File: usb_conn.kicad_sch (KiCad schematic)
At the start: 16 parts, among them U13 DLM0NSN500HY2D, U6 TPUSBLC6-4SC6

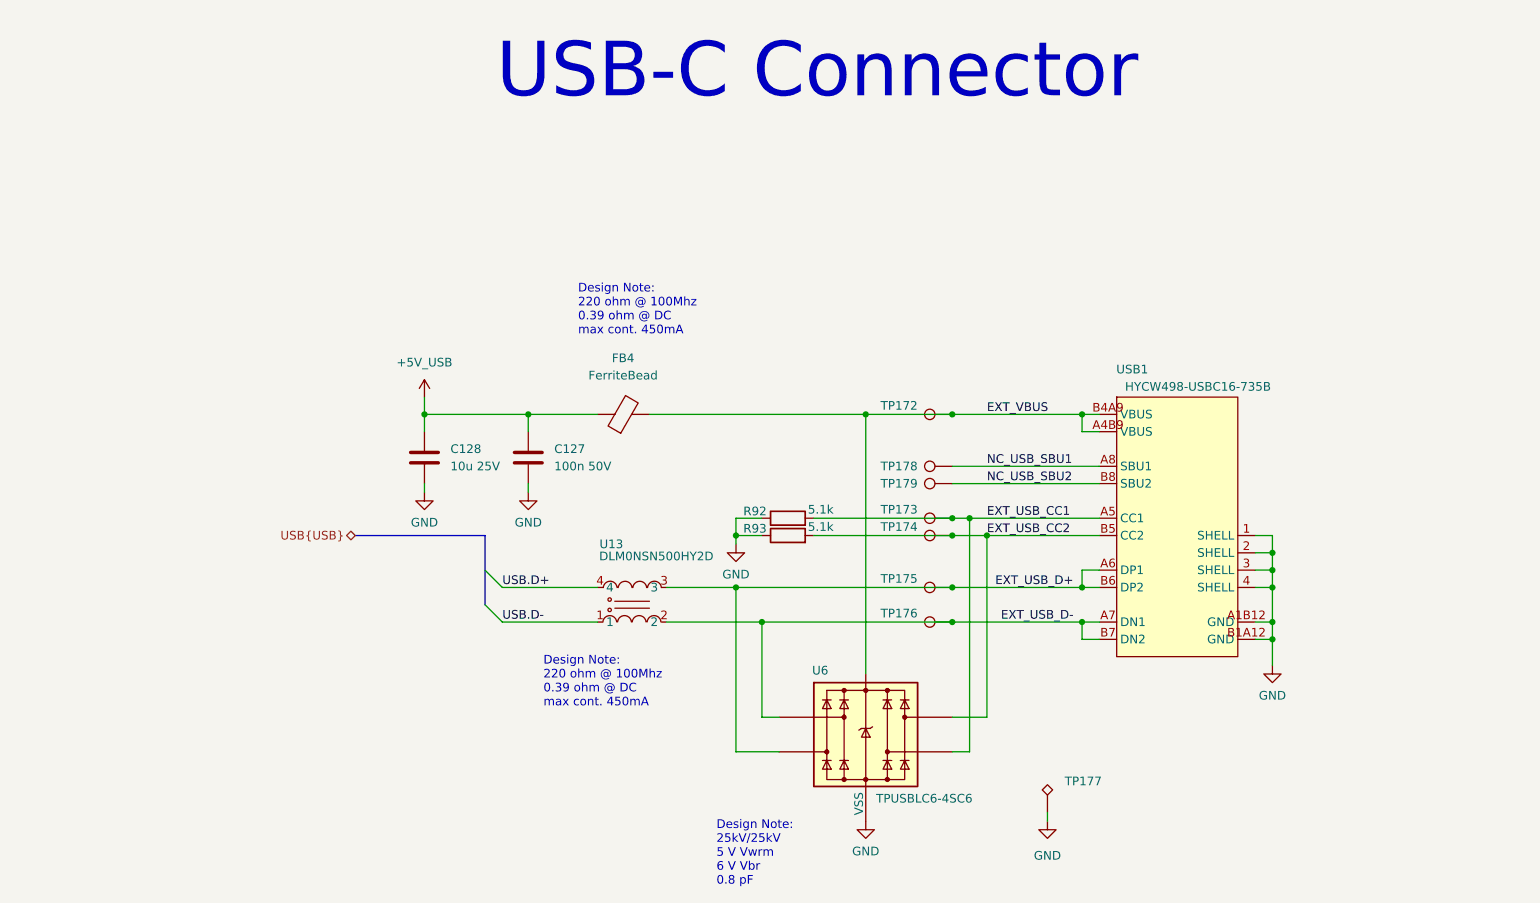
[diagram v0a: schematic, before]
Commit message: did stuff, amongst others changed to op-amp input filter
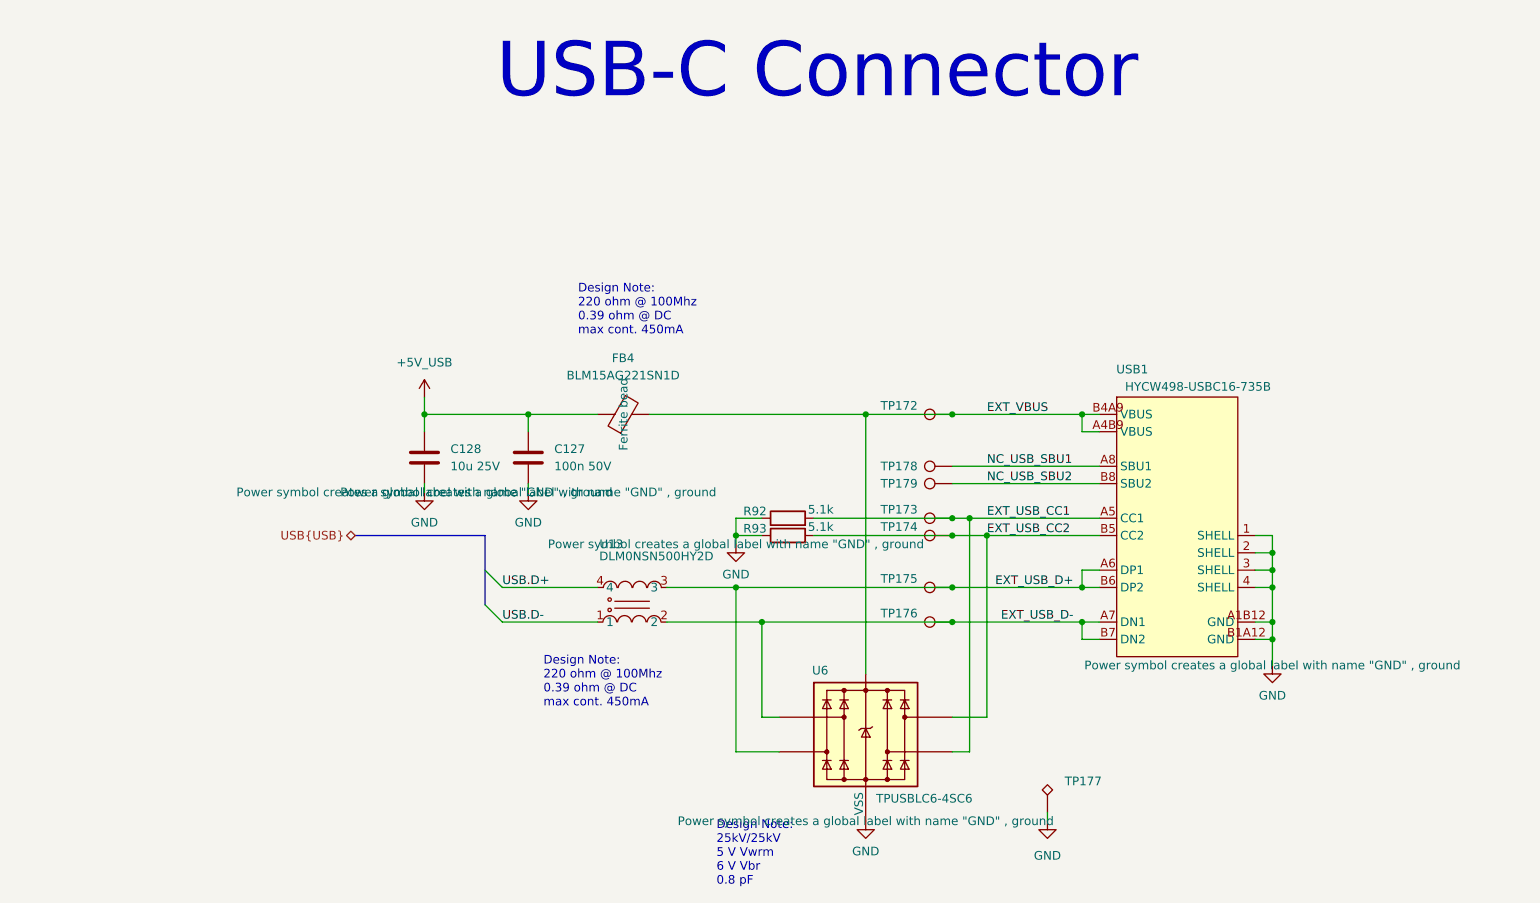
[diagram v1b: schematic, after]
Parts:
- FB4: value FerriteBead -> BLM15AG221SN1D; LCSC Part (none) -> C85813
- U13: LCSC (none) -> C913480
- USB1: LCSC (none) -> C42400252
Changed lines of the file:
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@@
+			)
+		)
+		(property "Tolerance" ""
+			(at 170.18 116.84 90)
+			(hide yes)
+			(show_name no)
+			(do_not_autoplace no)
+			(effects
+				(font
+					(size 1.27 1.27)
+				)
 			)
 		)
@@
 			)
 		)
-		(property "Description" ""
+		(property "Description" "Power symbol creates a global label with name \"GND\" , ground"
 			(at 92.71 97.79 0)
 			(show_name no)
@@
 			)
 		)
-		(property "Description" ""
+		(property "Description" "Power symbol creates a global label with name \"GND\" , ground"
 			(at 157.48 146.05 0)
 			(show_name no)
@@
 			)
 		)
-		(property "Description" ""
+		(property "Description" "Power symbol creates a global label with name \"GND\" , ground"
 			(at 217.17 123.19 0)
 			(show_name no)
@@
 			)
 		)
+		(property "Tolerance" ""
+			(at 170.18 86.36 90)
+			(hide yes)
+			(show_name no)
+			(do_not_autoplace no)
+			(effects
+				(font
+					(size 1.27 1.27)
+				)
+			)
+		)
 		(pin "1"
 		)
@@
 			)
 		)
-		(property "Description" ""
+		(property "Description" "Power symbol creates a global label with name \"GND\" , ground"
 			(at 107.95 97.79 0)
 			(show_name no)
@@
 		)
 		(property "LCSC missing" ""
+			(at 184.15 144.78 0)
+			(hide yes)
+			(show_name no)
+			(do_not_autoplace no)
+			(effects
+				(font
+					(size 1.27 1.27)
+				)
+			)
+		)
+		(property "Tolerance" ""
 			(at 184.15 144.78 0)
 			(hide yes)
@@
 			)
 		)
+		(property "Tolerance" ""
+			(at 170.18 111.76 90)
+			(hide yes)
+			(show_name no)
+			(do_not_autoplace no)
+			(effects
+				(font
+					(size 1.27 1.27)
+				)
+			)
+		)
 		(pin "1"
 		)
@@
 			)
 		)
+		(property "Tolerance" ""
+			(at 170.18 96.52 90)
+			(hide yes)
+			(show_name no)
+			(do_not_autoplace no)
+			(effects
+				(font
+					(size 1.27 1.27)
+				)
+			)
+		)
 		(pin "1"
 		)
@@
 			)
 		)
+		(property "Tolerance" ""
+			(at 107.95 92.71 0)
+			(hide yes)
+			(show_name no)
+			(do_not_autoplace no)
+			(effects
+				(font
+					(size 1.27 1.27)
+				)
+			)
+		)
 		(pin "1"
 		)
@@
 		)
 		(property "LCSC missing" ""
+			(at 146.05 104.14 90)
+			(hide yes)
+			(show_name no)
+			(do_not_autoplace no)
+			(effects
+				(font
+					(size 1.27 1.27)
+				)
+			)
+		)
+		(property "Tolerance" ""
 			(at 146.05 104.14 90)
 			(hide yes)
@@
 			)
 		)
+		(property "Tolerance" ""
+			(at 170.18 101.6 90)
+			(hide yes)
+			(show_name no)
+			(do_not_autoplace no)
+			(effects
+				(font
+					(size 1.27 1.27)
+				)
+			)
+		)
 		(pin "1"
 		)
@@
 			)
 		)
-		(property "Description" ""
+		(property "Description" "Power symbol creates a global label with name \"GND\" , ground"
 			(at 138.43 105.41 0)
 			(show_name no)
@@
 		)
 		(property "LCSC missing" ""
+			(at 123.19 114.3 0)
+			(hide yes)
+			(show_name no)
+			(do_not_autoplace no)
+			(effects
+				(font
+					(size 1.27 1.27)
+				)
+			)
+		)
+		(property "LCSC" "C913480"
+			(at 123.19 114.3 0)
+			(hide yes)
+			(show_name no)
+			(do_not_autoplace no)
+			(effects
+				(font
+					(size 1.27 1.27)
+				)
+			)
+		)
+		(property "Tolerance" ""
 			(at 123.19 114.3 0)
 			(hide yes)
@@
 			)
 		)
+		(property "Tolerance" ""
+			(at 170.18 104.14 90)
+			(hide yes)
+			(show_name no)
+			(do_not_autoplace no)
+			(effects
+				(font
+					(size 1.27 1.27)
+				)
+			)
+		)
 		(pin "1"
 		)
@@
 		)
 		(property "LCSC missing" ""
+			(at 157.48 133.35 0)
+			(hide yes)
+			(show_name no)
+			(do_not_autoplace no)
+			(effects
+				(font
+					(size 1.27 1.27)
+				)
+			)
+		)
+		(property "Tolerance" ""
 			(at 157.48 133.35 0)
 			(hide yes)
@@
 			)
 		)
-		(property "Value" "FerriteBead"
+		(property "Value" "BLM15AG221SN1D"
 			(at 121.8692 80.645 90)
 			(show_name no)
@@
 			)
 		)
-		(property "Description" ""
+		(property "Description" "Ferrite bead"
 			(at 121.92 86.36 0)
 			(show_name no)
@@
 		)
 		(property "LCSC missing" ""
+			(at 121.92 86.36 90)
+			(hide yes)
+			(show_name no)
+			(do_not_autoplace no)
+			(effects
+				(font
+					(size 1.27 1.27)
+				)
+			)
+		)
+		(property "LCSC Part" "C85813"
+			(at 121.92 86.36 90)
+			(hide yes)
+			(show_name no)
+			(do_not_autoplace no)
+			(effects
+				(font
+					(size 1.27 1.27)
+				)
+			)
+		)
+		(property "Tolerance" ""
 			(at 121.92 86.36 90)
 			(hide yes)
@@
 		)
 		(property "LCSC missing" ""
+			(at 146.05 101.6 90)
+			(hide yes)
+			(show_name no)
+			(do_not_autoplace no)
+			(effects
+				(font
+					(size 1.27 1.27)
+				)
+			)
+		)
+		(property "Tolerance" ""
 			(at 146.05 101.6 90)
 			(hide yes)
@@
 			)
 		)
+		(property "Tolerance" ""
+			(at 92.71 92.71 0)
+			(hide yes)
+			(show_name no)
+			(do_not_autoplace no)
+			(effects
+				(font
+					(size 1.27 1.27)
+				)
+			)
+		)
 		(pin "1"
 		)
@@
 		)
 		(property "LCSC missing" ""
+			(at 203.2 113.03 0)
+			(hide yes)
+			(show_name no)
+			(do_not_autoplace no)
+			(effects
+				(font
+					(size 1.27 1.27)
+				)
+			)
+		)
+		(property "LCSC" "C42400252"
+			(at 203.2 113.03 0)
+			(hide yes)
+			(show_name no)
+			(do_not_autoplace no)
+			(effects
+				(font
+					(size 1.27 1.27)
+				)
+			)
+		)
+		(property "Tolerance" ""
 			(at 203.2 113.03 0)
 			(hide yes)
@@
 			(at 170.18 93.98 90)
 			(hide yes)
+			(show_name no)
+			(do_not_autoplace no)
+			(effects
+				(font
+					(size 1.27 1.27)
+				)
+			)
+		)
+		(property "Tolerance" ""
+			(at 170.18 93.98 90)
+			(hide yes)

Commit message: fixed a bunch of errors, set pin type on alot of pins
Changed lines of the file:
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@@
 		(in_pos_files yes)
 		(dnp no)
-		(fields_autoplaced yes)
 		(property "Reference" "#PWR0293"
 			(at 92.71 104.14 0)
@@
 		)
 		(property "Description" "Power symbol creates a global label with name \"GND\" , ground"
-			(at 92.71 97.79 0)
+			(at 73.152 95.25 0)
+			(hide yes)
 			(show_name no)
 			(do_not_autoplace no)
@@
 		(property "Description" "Power symbol creates a global label with name \"GND\" , ground"
 			(at 157.48 146.05 0)
+			(hide yes)
 			(show_name no)
 			(do_not_autoplace no)
@@
 		(property "Description" "Power symbol creates a global label with name \"GND\" , ground"
 			(at 217.17 123.19 0)
+			(hide yes)
 			(show_name no)
 			(do_not_autoplace no)
@@
 		(property "Description" "Power symbol creates a global label with name \"GND\" , ground"
 			(at 107.95 97.79 0)
+			(hide yes)
 			(show_name no)
 			(do_not_autoplace no)
@@
 		(property "Description" "Power symbol creates a global label with name \"GND\" , ground"
 			(at 138.43 105.41 0)
+			(hide yes)
 			(show_name no)
 			(do_not_autoplace no)
@@
 		(property "Description" "Ferrite bead"
 			(at 121.92 86.36 0)
-			(show_name no)
-			(do_not_autoplace no)
+			(hide yes)
+			(show_name no)
+			(do_not_autoplace no)

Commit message: fixed a lot of review comments
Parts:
- FB4: MPN (none) -> BLM15AG221SN1D; Manufacturer (none) -> Murata
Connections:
- no-connect marks 0 -> 2
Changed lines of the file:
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@@
 		(color 0 0 0 0)
 	)
+	(no_connect
+		(at 106.68 130.81)
+	)
+	(no_connect
+		(at 33.02 139.7)
+	)
 	(bus_entry
 		(at 101.6 114.3)
@@
 			(at 121.92 86.36 90)
 			(hide yes)
+			(show_name no)
+			(do_not_autoplace no)
+			(effects
+				(font
+					(size 1.27 1.27)
+				)
+			)
+		)
+		(property "Manufacturer" "Murata"
+			(at 121.92 86.36 90)
+			(hide yes)
+			(show_name no)
+			(do_not_autoplace no)
+			(effects
+				(font
+					(size 1.27 1.27)
+				)
+			)
+		)
+		(property "MPN" "BLM15AG221SN1D"
+			(at 121.92 86.36 90)
+			(hide yes)
